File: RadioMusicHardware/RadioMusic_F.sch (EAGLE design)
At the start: 30 parts, among them X1 VERT_SD_CARD_REV2

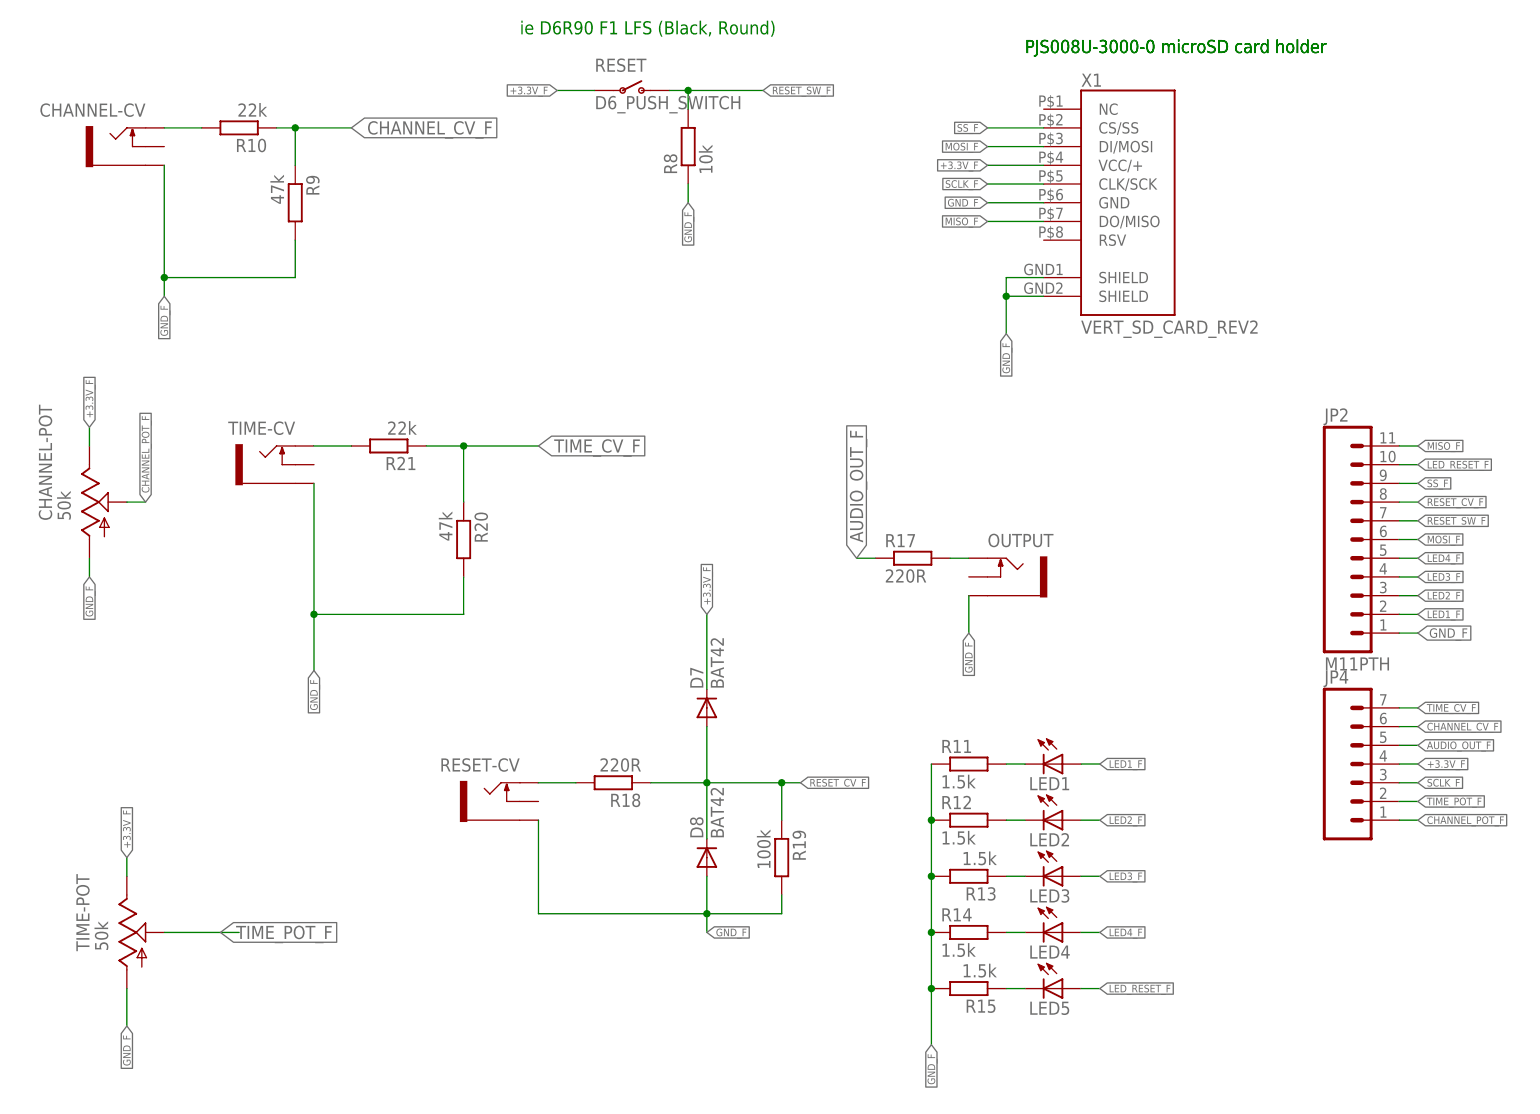
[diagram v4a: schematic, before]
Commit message: Layout experiments - back board output not completed
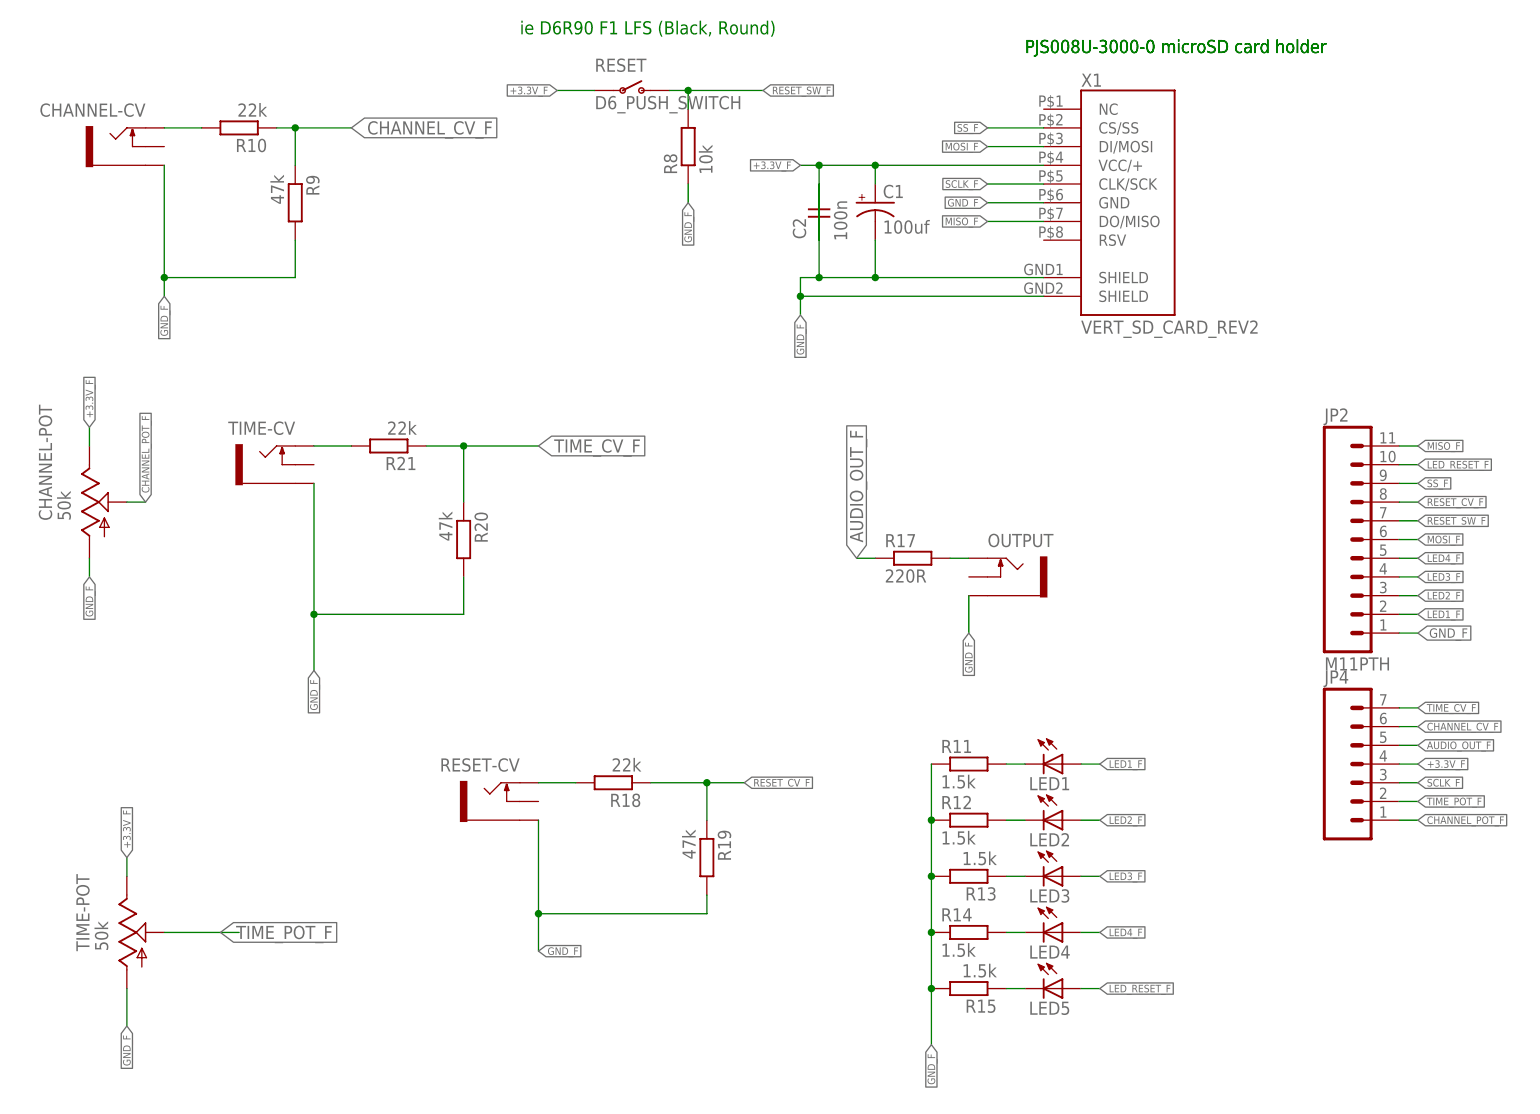
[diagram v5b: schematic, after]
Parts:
- removed D7, D8: BAT42, diode:BAT81
- added C1: 100uf, gm-caps-electro-pol:050
- added C2: 100n, TomW:C-EU050-024X044
- R18: value 220R -> 22k
- R19: value 100k -> 47k
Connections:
- net +3.3V_F: now also C1.+, C2.2; no longer D7.C
- net GND_F: now also C1.-, C2.1; no longer D8.A
- net RESET_CV_F: no longer D7.A, D8.C
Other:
- moved on the sheet: R19
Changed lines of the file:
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@@
 <?xml version="1.0" encoding="utf-8"?>
 <!DOCTYPE eagle SYSTEM "eagle.dtd">
-<eagle version="7.2.0">
+<eagle version="7.4.0">
 <drawing>
 <settings>
@@
 <part name="R20" library="MusicThingModular" deviceset="RESISTOR" device="VERTICAL" value="47k"/>
 <part name="R21" library="MusicThingModular" deviceset="RESISTOR" device="VERTICAL" value="22k"/>
-<part name="D7" library="diode" deviceset="BAT81" device="" value="BAT42"/>
-<part name="D8" library="diode" deviceset="BAT81" device="" value="BAT42"/>
-<part name="R19" library="MusicThingModular" deviceset="RESISTOR" device="7MM" value="100k"/>
-<part name="R18" library="MusicThingModular" deviceset="RESISTOR" device="7MM" value="220R"/>
+<part name="R19" library="MusicThingModular" deviceset="RESISTOR" device="7MM" value="47k"/>
+<part name="R18" library="MusicThingModular" deviceset="RESISTOR" device="7MM" value="22k"/>
 <part name="RESET" library="TomW" deviceset="D6_PUSH_SWITCH" device="" value="D6_PUSH_SWITCH"/>
 <part name="R8" library="MusicThingModular" deviceset="RESISTOR" device="7MM" value="10k"/>
@@
 <part name="JP2" library="SparkFun-Connectors" deviceset="M11" device="PTH" value="M11PTH"/>
 <part name="JP4" library="SparkFun-Connectors" deviceset="M07" device=""/>
+<part name="C1" library="gm-caps-electro-pol" deviceset="050" device="" value="100uf"/>
+<part name="C2" library="TomW" deviceset="C-EU" device="050-024X044" value="100n"/>
 </parts>
 <sheets>
@@
 <instance part="R20" gate="G$1" x="76.2" y="76.2" rot="R270"/>
 <instance part="R21" gate="G$1" x="66.04" y="88.9" rot="R180"/>
-<instance part="D7" gate="1" x="109.22" y="53.34" rot="R90"/>
-<instance part="D8" gate="1" x="109.22" y="33.02" rot="R90"/>
-<instance part="R19" gate="G$1" x="119.38" y="33.02" rot="R270"/>
+<instance part="R19" gate="G$1" x="109.22" y="33.02" rot="R270"/>
 <instance part="R18" gate="G$1" x="96.52" y="43.18" rot="R180"/>
 <instance part="RESET" gate="G$1" x="99.06" y="137.16"/>
@@
 <instance part="JP2" gate="G$1" x="193.04" y="76.2"/>
 <instance part="JP4" gate="G$1" x="198.12" y="43.18"/>
+<instance part="C1" gate="1" x="132.08" y="121.92"/>
+<instance part="C2" gate="G$1" x="124.46" y="121.92"/>
 </instances>
 <busses>
@@
 <segment>
 <pinref part="X1" gate="G$1" pin="VCC/+"/>
-<wire x1="147.32" y1="127" x2="154.94" y2="127" width="0.1524" layer="91"/>
-<label x="147.32" y="127" size="1.016" layer="95" rot="R180" xref="yes"/>
+<wire x1="121.92" y1="127" x2="124.46" y2="127" width="0.1524" layer="91"/>
+<label x="121.92" y="127" size="1.016" layer="95" rot="R180" xref="yes"/>
+<pinref part="C2" gate="G$1" pin="2"/>
+<wire x1="124.46" y1="127" x2="132.08" y2="127" width="0.1524" layer="91"/>
+<wire x1="132.08" y1="127" x2="154.94" y2="127" width="0.1524" layer="91"/>
+<wire x1="124.46" y1="116.84" x2="124.46" y2="127" width="0.1524" layer="91"/>
+<junction x="124.46" y="127"/>
+<pinref part="C1" gate="1" pin="+"/>
+<wire x1="132.08" y1="124.46" x2="132.08" y2="127" width="0.1524" layer="91"/>
+<junction x="132.08" y="127"/>
 </segment>
 <segment>
@@
 </segment>
 <segment>
-<pinref part="D7" gate="1" pin="C"/>
-<wire x1="109.22" y1="55.88" x2="109.22" y2="66.04" width="0.1524" layer="91"/>
-<label x="109.22" y="66.04" size="1.016" layer="95" rot="R90" xref="yes"/>
-</segment>
-<segment>
 <pinref part="RESET" gate="G$1" pin="P"/>
 <wire x1="88.9" y1="137.16" x2="93.98" y2="137.16" width="0.1524" layer="91"/>
@@
 </segment>
 <segment>
-<wire x1="149.86" y1="104.14" x2="149.86" y2="109.22" width="0.1524" layer="91"/>
+<wire x1="121.92" y1="106.68" x2="121.92" y2="109.22" width="0.1524" layer="91"/>
 <pinref part="X1" gate="G$1" pin="SHIELD@1"/>
-<wire x1="149.86" y1="109.22" x2="149.86" y2="111.76" width="0.1524" layer="91"/>
-<wire x1="149.86" y1="111.76" x2="154.94" y2="111.76" width="0.1524" layer="91"/>
+<wire x1="121.92" y1="109.22" x2="121.92" y2="111.76" width="0.1524" layer="91"/>
+<wire x1="121.92" y1="111.76" x2="124.46" y2="111.76" width="0.1524" layer="91"/>
 <pinref part="X1" gate="G$1" pin="SHIELD@2"/>
-<wire x1="154.94" y1="109.22" x2="149.86" y2="109.22" width="0.1524" layer="91"/>
-<junction x="149.86" y="109.22"/>
-<label x="149.86" y="104.14" size="1.016" layer="95" rot="R270" xref="yes"/>
+<wire x1="124.46" y1="111.76" x2="132.08" y2="111.76" width="0.1524" layer="91"/>
+<wire x1="132.08" y1="111.76" x2="154.94" y2="111.76" width="0.1524" layer="91"/>
+<wire x1="154.94" y1="109.22" x2="121.92" y2="109.22" width="0.1524" layer="91"/>
+<junction x="121.92" y="109.22"/>
+<label x="121.92" y="106.68" size="1.016" layer="95" rot="R270" xref="yes"/>
+<pinref part="C1" gate="1" pin="-"/>
+<wire x1="132.08" y1="116.84" x2="132.08" y2="111.76" width="0.1524" layer="91"/>
+<junction x="132.08" y="111.76"/>
+<pinref part="C2" gate="G$1" pin="1"/>
+<wire x1="124.46" y1="124.46" x2="124.46" y2="111.76" width="0.1524" layer="91"/>
+<junction x="124.46" y="111.76"/>
 </segment>
 <segment>
@@
 <wire x1="86.36" y1="38.1" x2="86.36" y2="25.4" width="0.1524" layer="91"/>
 <pinref part="R19" gate="G$1" pin="2"/>
-<wire x1="119.38" y1="27.94" x2="119.38" y2="25.4" width="0.1524" layer="91"/>
-<pinref part="D8" gate="1" pin="A"/>
-<wire x1="109.22" y1="25.4" x2="109.22" y2="30.48" width="0.1524" layer="91"/>
-<wire x1="119.38" y1="25.4" x2="109.22" y2="25.4" width="0.1524" layer="91"/>
-<wire x1="86.36" y1="25.4" x2="109.22" y2="25.4" width="0.1524" layer="91"/>
-<junction x="109.22" y="25.4"/>
-<wire x1="109.22" y1="25.4" x2="109.22" y2="22.86" width="0.1524" layer="91"/>
-<label x="109.22" y="22.86" size="1.016" layer="95" xref="yes"/>
+<wire x1="109.22" y1="27.94" x2="109.22" y2="25.4" width="0.1524" layer="91"/>
+<wire x1="109.22" y1="25.4" x2="86.36" y2="25.4" width="0.1524" layer="91"/>
+<junction x="86.36" y="25.4"/>
+<wire x1="86.36" y1="25.4" x2="86.36" y2="20.32" width="0.1524" layer="91"/>
+<label x="86.36" y="20.32" size="1.016" layer="95" xref="yes"/>
 </segment>
 <segment>
@@
 <net name="RESET_CV_F" class="0">
 <segment>
-<pinref part="D7" gate="1" pin="A"/>
-<pinref part="D8" gate="1" pin="C"/>
-<wire x1="109.22" y1="35.56" x2="109.22" y2="43.18" width="0.1524" layer="91"/>
 <pinref part="R18" gate="G$1" pin="1"/>
-<wire x1="109.22" y1="43.18" x2="109.22" y2="50.8" width="0.1524" layer="91"/>
 <wire x1="101.6" y1="43.18" x2="109.22" y2="43.18" width="0.1524" layer="91"/>
+<pinref part="R19" gate="G$1" pin="1"/>
+<wire x1="109.22" y1="43.18" x2="114.3" y2="43.18" width="0.1524" layer="91"/>
+<wire x1="109.22" y1="38.1" x2="109.22" y2="43.18" width="0.1524" layer="91"/>
 <junction x="109.22" y="43.18"/>
-<wire x1="109.22" y1="43.18" x2="119.38" y2="43.18" width="0.1524" layer="91"/>
-<pinref part="R19" gate="G$1" pin="1"/>
-<wire x1="119.38" y1="43.18" x2="121.92" y2="43.18" width="0.1524" layer="91"/>
-<wire x1="119.38" y1="38.1" x2="119.38" y2="43.18" width="0.1524" layer="91"/>
-<junction x="119.38" y="43.18"/>
-<label x="121.92" y="43.18" size="1.016" layer="95" xref="yes"/>
-</segment>
-<segment>
+<label x="114.3" y="43.18" size="1.016" layer="95" xref="yes"/>
+</segment>
+<segment>
